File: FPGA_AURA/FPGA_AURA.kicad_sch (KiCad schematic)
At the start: 0 parts

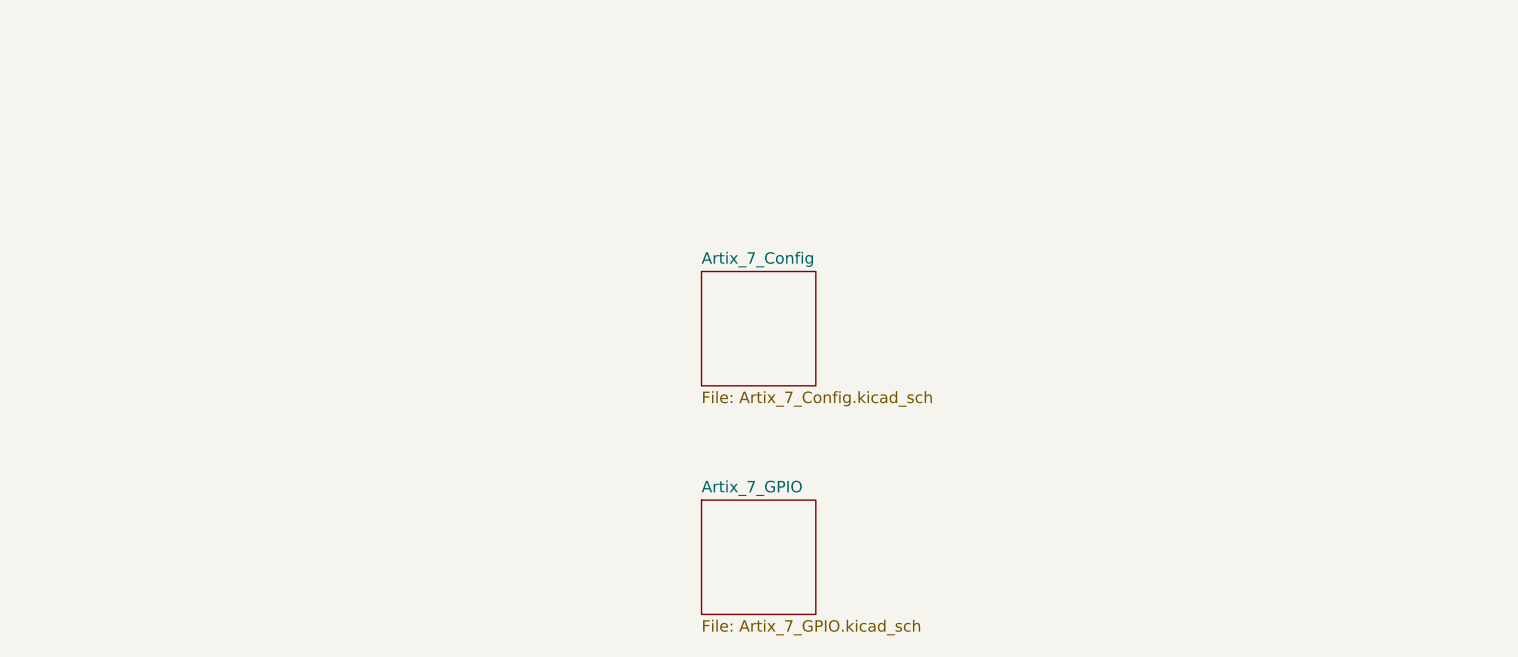
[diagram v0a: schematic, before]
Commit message: Power regulation started
Started doing research into the project to see what needs to be done
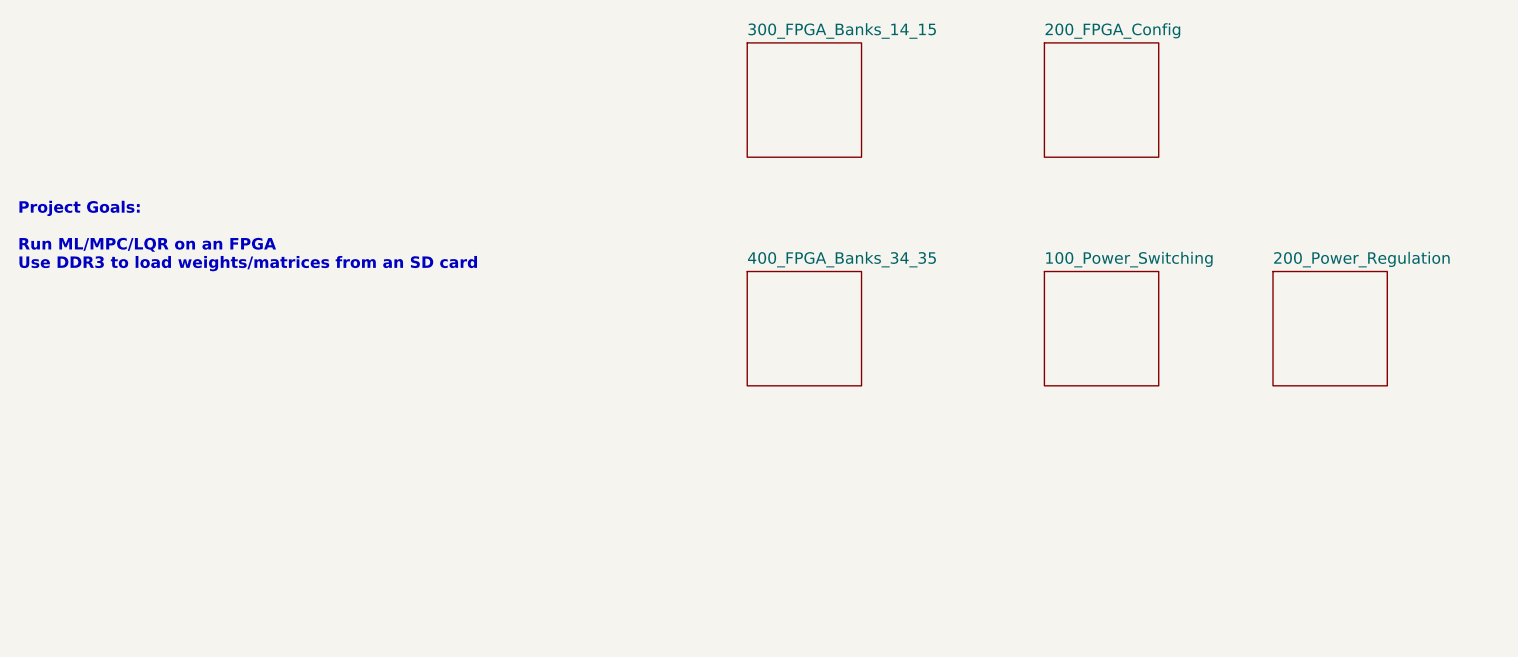
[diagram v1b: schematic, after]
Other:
- sheet Artix_7_Config renamed 300_FPGA_Banks_14_15
- sheet Artix_7_GPIO renamed 400_FPGA_Banks_34_35
- added sheet 100_Power_Switching (100_Power_Switching.kicad_sch)
- added sheet 200_FPGA_Config (200_FPGA_Config.kicad_sch)
- added sheet 200_Power_Regulation (200_Power_Regulation.kicad_sch)
- sheet 300_FPGA_Banks_14_15: file Artix_7_Config.kicad_sch -> 300_FPGA_Banks_14_15.kicad_sch
- sheet 400_FPGA_Banks_34_35: file Artix_7_GPIO.kicad_sch -> 400_FPGA_Banks_34_35.kicad_sch
- note added: "Project Goals: Run ML/MPC/LQR on an FPGA Use DDR3 to load weights/matrices from an SD card"
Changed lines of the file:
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@@
 	(generator_version "9.0")
 	(paper "A4")
-	(sheet
-		(at 139.7 114.3)
-		(size 12.7 12.7)
-		(exclude_from_sim no)
-		(in_bom yes)
-		(on_board yes)
-		(dnp no)
-		(fields_autoplaced yes)
-		(stroke
-			(width 0.1524)
-			(type solid)
-		)
-		(fill
-			(color 0 0 0 0.0000)
-		)
-		(property "Sheetname" "Artix_7_GPIO"
-			(at 139.7 113.5884 0)
-			(effects
-				(font
-					(size 1.27 1.27)
-				)
-				(justify left bottom)
-			)
-		)
-		(property "Sheetfile" "Artix_7_GPIO.kicad_sch"
-			(at 139.7 127.5846 0)
-			(effects
-				(font
-					(size 1.27 1.27)
-				)
-				(justify left top)
+	(text "Project Goals:\n\nRun ML/MPC/LQR on an FPGA\nUse DDR3 to load weights/matrices from an SD card\n"
+		(exclude_from_sim no)
+		(at 63.754 88.9 0)
+		(effects
+			(font
+				(size 1.27 1.27)
+				(thickness 0.254)
+				(bold yes)
+			)
+			(justify left bottom)
+		)
+	)
+	(sheet
+		(at 203.2 88.9)
+		(size 12.7 12.7)
+		(exclude_from_sim no)
+		(in_bom yes)
+		(on_board yes)
+		(dnp no)
+		(fields_autoplaced yes)
+		(stroke
+			(width 0.1524)
+			(type solid)
+		)
+		(fill
+			(color 0 0 0 0.0000)
+		)
+		(property "Sheetname" "200_Power_Regulation"
+			(at 203.2 88.1884 0)
+			(effects
+				(font
+					(size 1.27 1.27)
+				)
+				(justify left bottom)
+			)
+		)
+		(property "Sheetfile" "200_Power_Regulation.kicad_sch"
+			(at 203.2 102.1846 0)
+			(effects
+				(font
+					(size 1.27 1.27)
+				)
+				(justify left top)
+				(hide yes)
+			)
+		)
+		(instances
+			(project "FPGA_AURA"
+				(path "/3d83cb23-9528-4d06-8969-599520e9eb23"
+					(page "2")
+				)
+			)
+		)
+	)
+	(sheet
+		(at 144.78 88.9)
+		(size 12.7 12.7)
+		(exclude_from_sim no)
+		(in_bom yes)
+		(on_board yes)
+		(dnp no)
+		(fields_autoplaced yes)
+		(stroke
+			(width 0.1524)
+			(type solid)
+		)
+		(fill
+			(color 0 0 0 0.0000)
+		)
+		(property "Sheetname" "400_FPGA_Banks_34_35"
+			(at 144.78 88.1884 0)
+			(effects
+				(font
+					(size 1.27 1.27)
+				)
+				(justify left bottom)
+			)
+		)
+		(property "Sheetfile" "400_FPGA_Banks_34_35.kicad_sch"
+			(at 144.78 102.1846 0)
+			(effects
+				(font
+					(size 1.27 1.27)
+				)
+				(justify left top)
+				(hide yes)
+			)
+		)
+		(instances
+			(project "FPGA_AURA"
+				(path "/3d83cb23-9528-4d06-8969-599520e9eb23"
+					(page "4")
+				)
+			)
+		)
+	)
+	(sheet
+		(at 144.78 63.5)
+		(size 12.7 12.7)
+		(exclude_from_sim no)
+		(in_bom yes)
+		(on_board yes)
+		(dnp no)
+		(fields_autoplaced yes)
+		(stroke
+			(width 0.1524)
+			(type solid)
+		)
+		(fill
+			(color 0 0 0 0.0000)
+		)
+		(property "Sheetname" "300_FPGA_Banks_14_15"
+			(at 144.78 62.7884 0)
+			(effects
+				(font
+					(size 1.27 1.27)
+				)
+				(justify left bottom)
+			)
+		)
+		(property "Sheetfile" "300_FPGA_Banks_14_15.kicad_sch"
+			(at 144.78 76.7846 0)
+			(effects
+				(font
+					(size 1.27 1.27)
+				)
+				(justify left top)
+				(hide yes)
 			)
 		)
@@
 	)
 	(sheet
-		(at 139.7 88.9)
-		(size 12.7 12.7)
-		(exclude_from_sim no)
-		(in_bom yes)
-		(on_board yes)
-		(dnp no)
-		(fields_autoplaced yes)
-		(stroke
-			(width 0.1524)
-			(type solid)
-		)
-		(fill
-			(color 0 0 0 0.0000)
-		)
-		(property "Sheetname" "Artix_7_Config"
-			(at 139.7 88.1884 0)
-			(effects
-				(font
-					(size 1.27 1.27)
-				)
-				(justify left bottom)
-			)
-		)
-		(property "Sheetfile" "Artix_7_Config.kicad_sch"
-			(at 139.7 102.1846 0)
-			(effects
-				(font
-					(size 1.27 1.27)
-				)
-				(justify left top)
+		(at 177.8 63.5)
+		(size 12.7 12.7)
+		(exclude_from_sim no)
+		(in_bom yes)
+		(on_board yes)
+		(dnp no)
+		(fields_autoplaced yes)
+		(stroke
+			(width 0.1524)
+			(type solid)
+		)
+		(fill
+			(color 0 0 0 0.0000)
+		)
+		(property "Sheetname" "200_FPGA_Config"
+			(at 177.8 62.7884 0)
+			(effects
+				(font
+					(size 1.27 1.27)
+				)
+				(justify left bottom)
+			)
+		)
+		(property "Sheetfile" "200_FPGA_Config.kicad_sch"
+			(at 177.8 76.7846 0)
+			(effects
+				(font
+					(size 1.27 1.27)
+				)
+				(justify left top)
+				(hide yes)
 			)
 		)
@@
 				)
 			)
+		)
+	)
+	(sheet
+		(at 177.8 88.9)
+		(size 12.7 12.7)
+		(exclude_from_sim no)
+		(in_bom yes)
+		(on_board yes)
+		(dnp no)
+		(fields_autoplaced yes)
+		(stroke
+			(width 0.1524)
+			(type solid)
+		)
+		(fill
+			(color 0 0 0 0.0000)
+		)
+		(property "Sheetname" "100_Power_Switching"
+			(at 177.8 88.1884 0)
+			(effects
+				(font
+					(size 1.27 1.27)
+				)
+				(justify left bottom)
+			)
+		)
+		(property "Sheetfile" "100_Power_Switching.kicad_sch"
+			(at 177.8 102.1846 0)
+			(effects
+				(font
+					(size 1.27 1.27)
+				)
+				(justify left top)
+				(hide yes)
+			)
+		)
+		(instances
+			(project "FPGA_AURA"
+				(path "/3d83cb23-9528-4d06-8969-599520e9eb23"
+					(page "1")
+				)
+			)

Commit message: Initial component selection done
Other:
- added sheet 500_DDR3L (500_DDR3L.kicad_sch)
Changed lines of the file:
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@@
+	)
+	(sheet
+		(at 203.2 114.3)
+		(size 12.7 12.7)
+		(exclude_from_sim no)
+		(in_bom yes)
+		(on_board yes)
+		(dnp no)
+		(fields_autoplaced yes)
+		(stroke
+			(width 0.1524)
+			(type solid)
+		)
+		(fill
+			(color 0 0 0 0.0000)
+		)
+		(property "Sheetname" "500_DDR3L"
+			(at 203.2 113.5884 0)
+			(effects
+				(font
+					(size 1.27 1.27)
+				)
+				(justify left bottom)
+			)
+		)
+		(property "Sheetfile" "500_DDR3L.kicad_sch"
+			(at 203.2 127.5846 0)
+			(effects
+				(font
+					(size 1.27 1.27)
+				)
+				(justify left top)
+			)
+		)
+		(instances
+			(project "FPGA_AURA"
+				(path "/3d83cb23-9528-4d06-8969-599520e9eb23"
+					(page "7")
+				)
+			)
+		)
 	)
 	(sheet

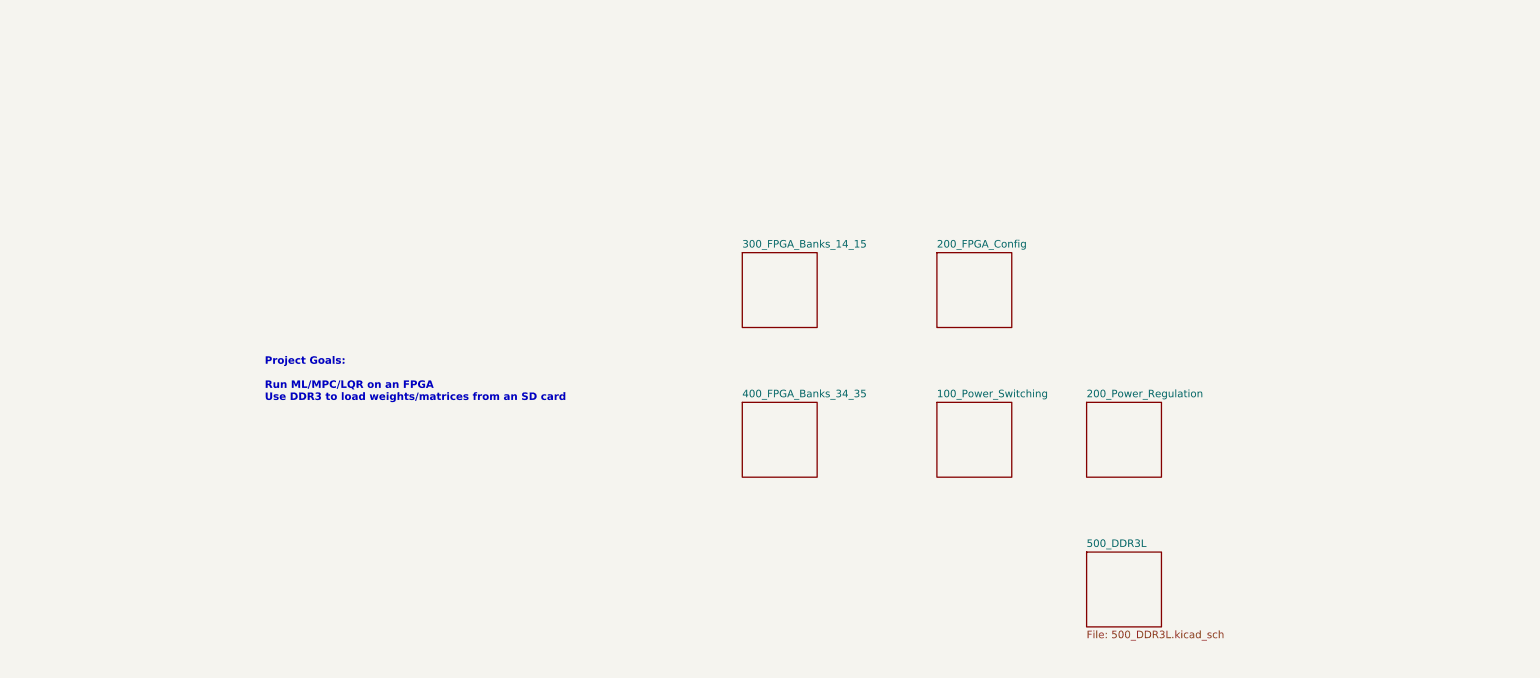
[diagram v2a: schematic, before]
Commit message: Added USB power schottky and started DDR3L
Transferring from laptop to PC to decide DDR3 pins.
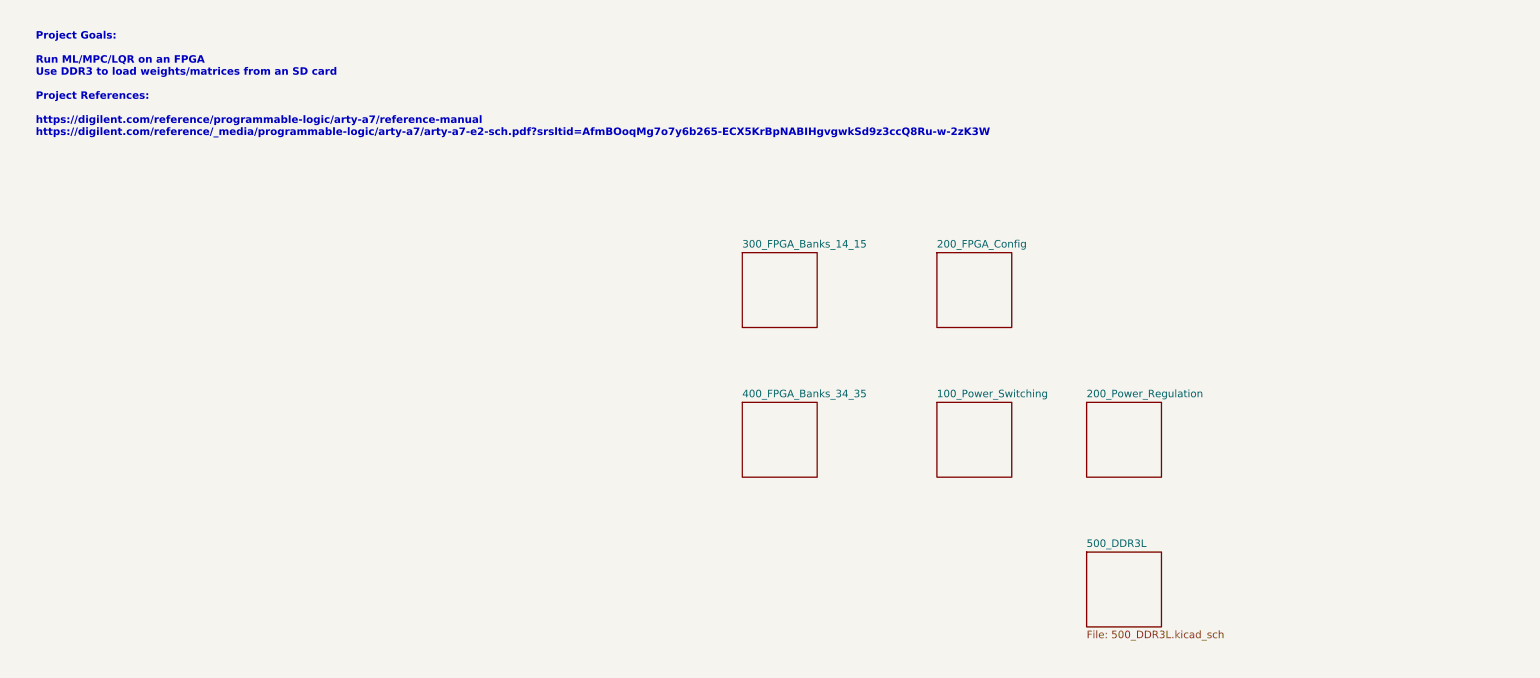
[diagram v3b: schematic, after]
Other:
- note added: "Project Goals: Run ML/MPC/LQR on an FPGA Use DDR3 to load weights/matrices from an SD card Project References: https://digilent.com/reference/programmable-logic/arty-a7/reference-manual https://digilent.com/reference/_media/programmable-logic/arty-a7/arty-a7-e2-sch.pdf?srsltid=AfmBOoqMg7o7y6b265-ECX5KrBpNABIHgvgwkSd9z3ccQ8Ru-w-2zK3W"
- note removed: "Project Goals: Run ML/MPC/LQR on an FPGA Use DDR3 to load weights/matrices from an SD card"
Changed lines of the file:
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@@
 	(generator_version "9.0")
 	(paper "A4")
-	(text "Project Goals:\n\nRun ML/MPC/LQR on an FPGA\nUse DDR3 to load weights/matrices from an SD card\n"
+	(text "Project Goals:\n\nRun ML/MPC/LQR on an FPGA\nUse DDR3 to load weights/matrices from an SD card\n\nProject References:\n\nhttps://digilent.com/reference/programmable-logic/arty-a7/reference-manual\nhttps://digilent.com/reference/_media/programmable-logic/arty-a7/arty-a7-e2-sch.pdf?srsltid=AfmBOoqMg7o7y6b265-ECX5KrBpNABIHgvgwkSd9z3ccQ8Ru-w-2zK3W\n"
 		(exclude_from_sim no)
-		(at 63.754 88.9 0)
+		(at 24.892 43.942 0)
 		(effects
 			(font

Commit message: Moving progress to laptop.
Started to decide on BGA fanout for DDR. Next is for the FPGA and to assign byte lanes to DQ.
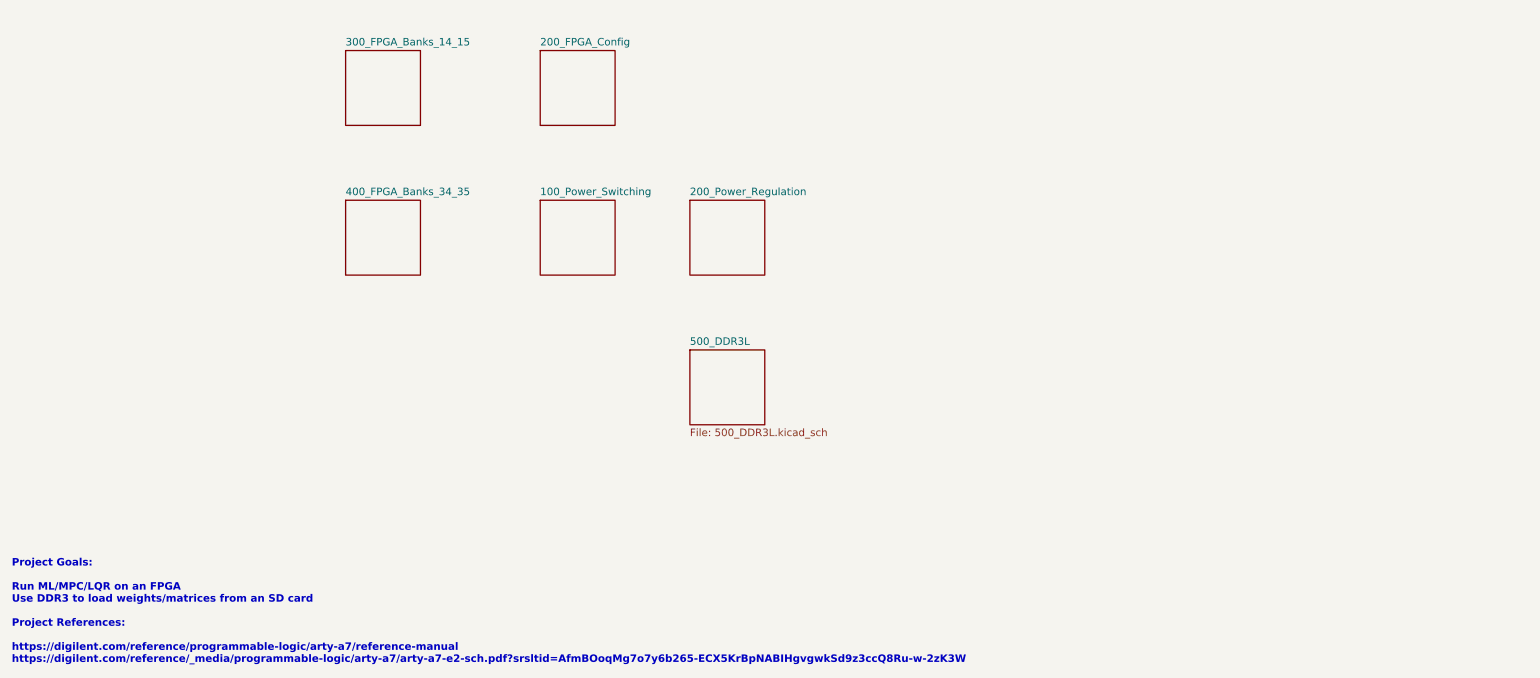
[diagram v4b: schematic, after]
